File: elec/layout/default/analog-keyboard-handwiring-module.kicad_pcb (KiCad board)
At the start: 2 copper layers, 95.2 x 95.2 mm, 524 parts

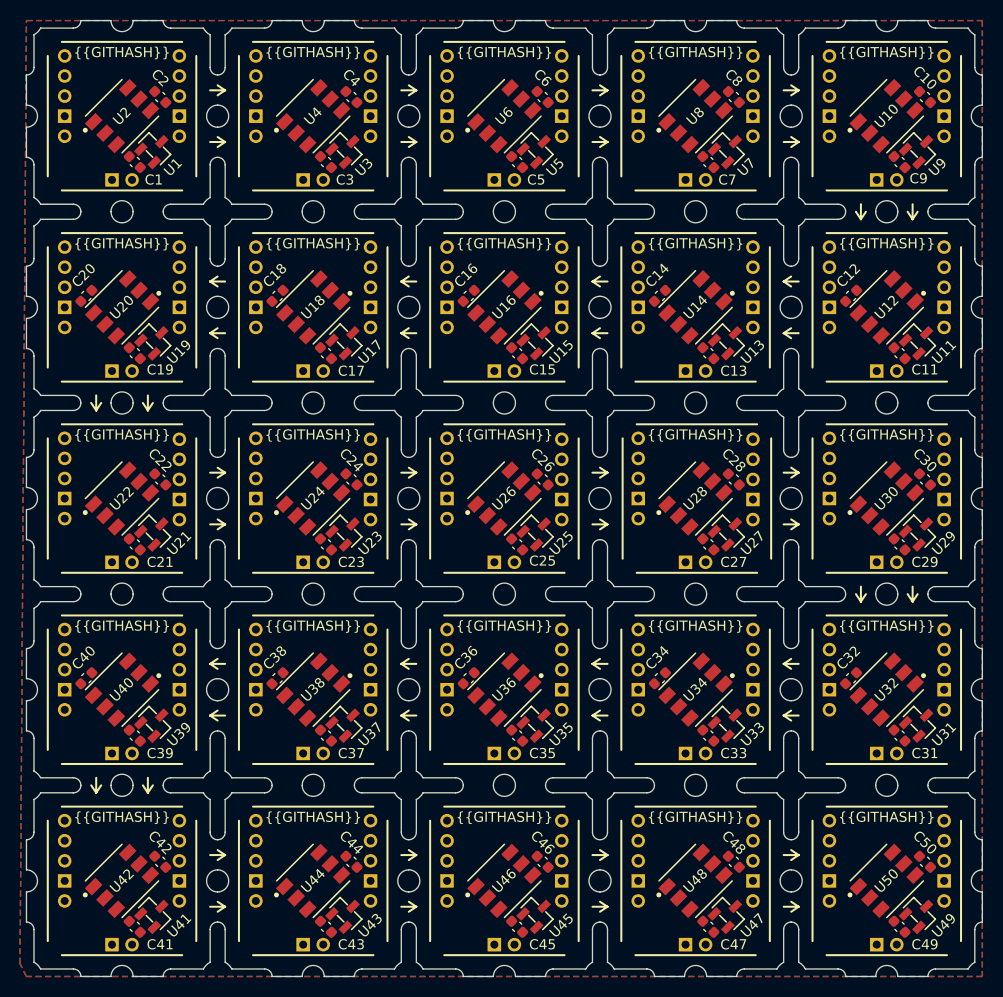
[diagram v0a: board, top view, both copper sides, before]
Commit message: Fix wrongly connected leds and start of layouting
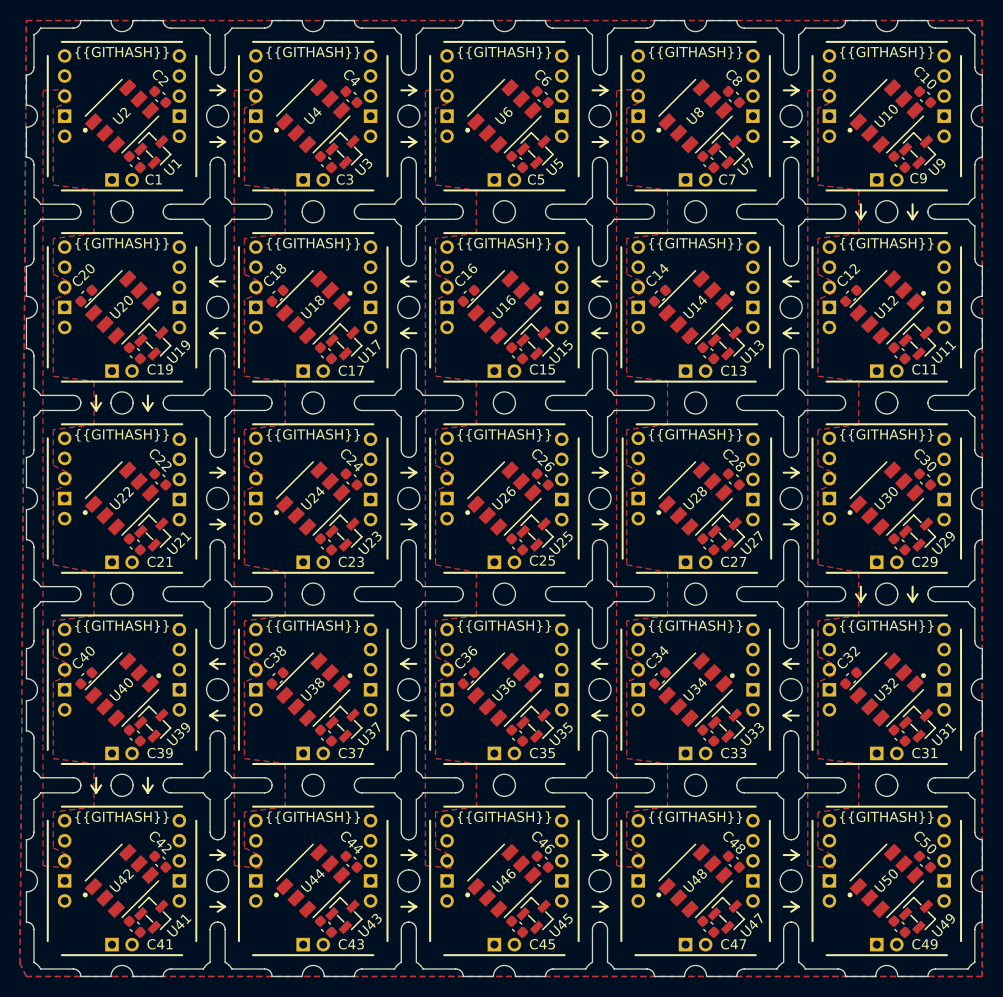
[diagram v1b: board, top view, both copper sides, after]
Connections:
- J11 pad 4: row1-ck -> row1.key4-ck
- J11 pad 5: row1-sd -> row1.key4-sd
- J13 pad 4: row1-ck -> row1.key4-ck
- J13 pad 5: row1-sd -> row1.key4-sd
- J14 pad 4: row1.key5-ck -> row1-ck
- J14 pad 5: row1.key5-sd -> row1-sd
- J26 pad 4: row2-ck -> row2.key4-ck
- J26 pad 5: row2-sd -> row2.key4-sd
- J28 pad 4: row2-ck -> row2.key4-ck
- J28 pad 5: row2-sd -> row2.key4-sd
- J29 pad 4: row2.key5-ck -> row2-ck
- J29 pad 5: row2.key5-sd -> row2-sd
- J41 pad 4: row3-ck -> row3.key4-ck
- J41 pad 5: row3-sd -> row3.key4-sd
- J43 pad 4: row3-ck -> row3.key4-ck
- J43 pad 5: row3-sd -> row3.key4-sd
- J44 pad 4: row3.key5-ck -> row3-ck
- J44 pad 5: row3.key5-sd -> row3-sd
- J56 pad 4: ck-1 -> row4.key4-ck
- J56 pad 5: sd-1 -> row4.key4-sd
- J58 pad 4: ck-1 -> row4.key4-ck
- J58 pad 5: sd-1 -> row4.key4-sd
- J59 pad 4: row4.key5-ck -> ck-1
- J59 pad 5: row4.key5-sd -> sd-1
- J71 pad 4: row5-ck -> row5.key4-ck
- J71 pad 5: row5-sd -> row5.key4-sd
- J73 pad 4: row5-ck -> row5.key4-ck
- J73 pad 5: row5-sd -> row5.key4-sd
- J74 pad 4: row5.key5-ck -> row5-ck
- J74 pad 5: row5.key5-sd -> row5-sd
- U10 pad 1: row1-sd -> row1.key4-sd
- U10 pad 2: row1-ck -> row1.key4-ck
- U10 pad 5: row1.key5-ck -> row1-ck
- U10 pad 6: row1.key5-sd -> row1-sd
- U18 pad 5: row2-ck -> row2.key4-ck
- U18 pad 6: row2-sd -> row2.key4-sd
- U20 pad 1: row2-sd -> row2.key4-sd
- U20 pad 2: row2-ck -> row2.key4-ck
- U20 pad 5: row2.key5-ck -> row2-ck
- U20 pad 6: row2.key5-sd -> row2-sd
- U28 pad 5: row3-ck -> row3.key4-ck
- U28 pad 6: row3-sd -> row3.key4-sd
- U30 pad 1: row3-sd -> row3.key4-sd
- U30 pad 2: row3-ck -> row3.key4-ck
- U30 pad 5: row3.key5-ck -> row3-ck
- U30 pad 6: row3.key5-sd -> row3-sd
- U38 pad 5: ck-1 -> row4.key4-ck
- U38 pad 6: sd-1 -> row4.key4-sd
- U40 pad 1: sd-1 -> row4.key4-sd
- U40 pad 2: ck-1 -> row4.key4-ck
- U40 pad 5: row4.key5-ck -> ck-1
- U40 pad 6: row4.key5-sd -> sd-1
- U48 pad 5: row5-ck -> row5.key4-ck
- U48 pad 6: row5-sd -> row5.key4-sd
- U50 pad 1: row5-sd -> row5.key4-sd
- U50 pad 2: row5-ck -> row5.key4-ck
- U50 pad 5: row5.key5-ck -> row5-ck
- U50 pad 6: row5.key5-sd -> row5-sd
- U8 pad 5: row1-ck -> row1.key4-ck
- U8 pad 6: row1-sd -> row1.key4-sd
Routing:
- added copper zone on F.Cu, net vccl
